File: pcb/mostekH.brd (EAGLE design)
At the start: 32 x 40.3 mm, 27 parts, among them Q1 BSS123, Q2 BSS123, Q3 BSS84, Q4 BSS84, T1 BC547, T2 BC547

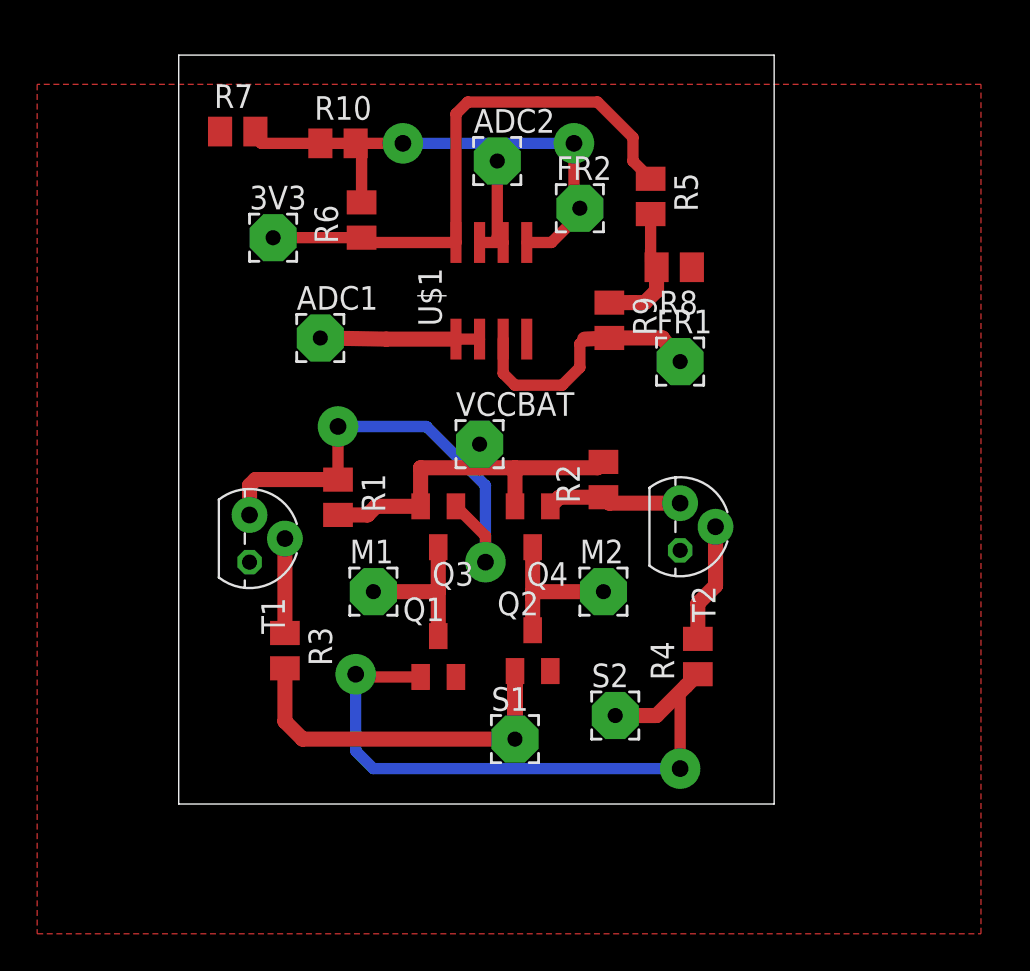
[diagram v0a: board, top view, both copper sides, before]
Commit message: postęp w mgr.doc, aktualizacja brd mostek H, GPS dev board
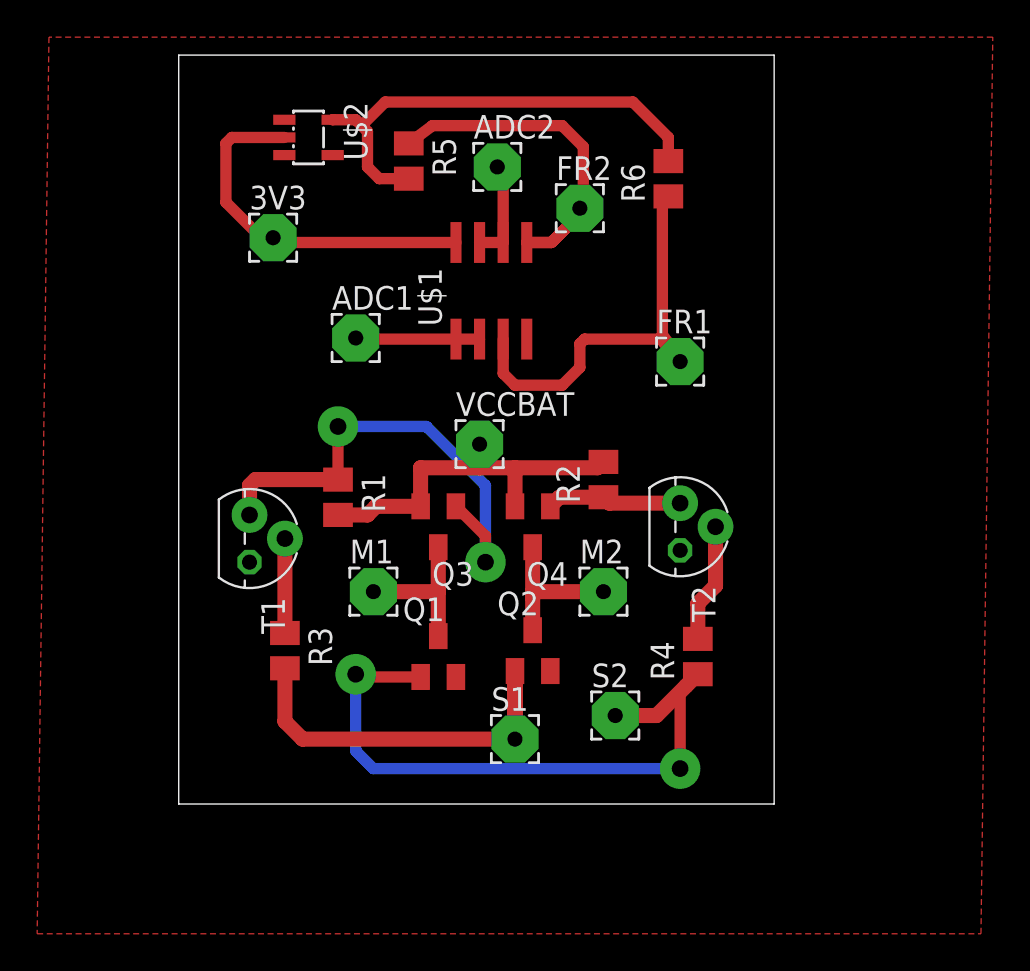
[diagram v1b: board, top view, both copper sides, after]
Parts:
- removed R10, R7, R8, R9: 50k, rcl:M0805
- added U$2: MAX6129, ref-packages:SOT23-5L
- Q1, Q2: value BSS123 -> AP2302
- Q3, Q4: value BSS84 -> AP2301
- moved R6 16.7 mm to (32.7, 40.6)
- moved R5 13.2 mm to (18.7, 41.6)
- moved ADC1 1.90 mm to (15.9, 32.1)
- moved ADC2 0.32 mm to (23.5, 41.3)
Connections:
- removed net N$14: R10.1, R6.2, R7.2
- net +3V3: now also U$2.2; no longer R5.1, R6.1
- net GND: no longer R7.1, R8.1
- net N$13: now also R6.2, U$2.5; no longer R8.2, R9.1
- net N$6: now also R6.1; no longer R9.2
- net N$8: now also R5.1; no longer R10.2
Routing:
- net N$13: track 7.07 -> 25.6 mm
- net +3V3: track 30.1 -> 19.7 mm
- net N$14: track 9.34 -> 0.00 mm
- net N$6: track 14.0 -> 21.8 mm
- net N$8: track 19.5 -> 21.5 mm, vias 2 -> 0
- net N$11: track 8.57 -> 6.69 mm
